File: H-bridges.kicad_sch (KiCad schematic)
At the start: 34 parts, among them J2 Conn_Coaxial, J3 Conn_Coaxial, Q10 NMOS, Q11 NMOS, Q12 NMOS, Q13 NMOS, Q14 NMOS, Q7 NMOS, Q8 NMOS, Q9 NMOS, U10 MIC4604YM, U11 MIC4604YM, U8 MIC4604YM, U9 MIC4604YM

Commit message: schematics done
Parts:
- removed D7, D8, D9: D, symbol Device:D
- added D1, D2, D5: 1N4148W, Diode_SMD:D_SOD-123, symbol Device:D
- added R1, R2: 0, Resistor_SMD:R_1206_3216Metric_Pad1.30x1.75mm_HandSolder, symbol Device:R
- D6: value D -> 1N4148W; footprint (none) -> Diode_SMD:D_SOD-123
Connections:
- net GND: now also D1.2 (A), D2.2 (A), D5.2 (A)
- net at C15.2, R35.1, U9.4 (HS): now also D1.1 (K)
- net at C14.2, R32.1, U8.4 (HS): now also D2.1 (K); no longer D6.1 (K)
- net at C16.2, R40.1, U10.4 (HS): now also D5.1 (K)
- net at C17.2, R41.1, U11.4 (HS): now also D6.1 (K)
- net P24V: no longer names the net of Q7.1 (D), Q9.1 (D)
- net P24V: now also R2.2; no longer Q11.1 (D), Q13.1 (D)
- new net: Q11.1 (D), Q13.1 (D), R1.2
- new net PHV: R1.1, R2.1

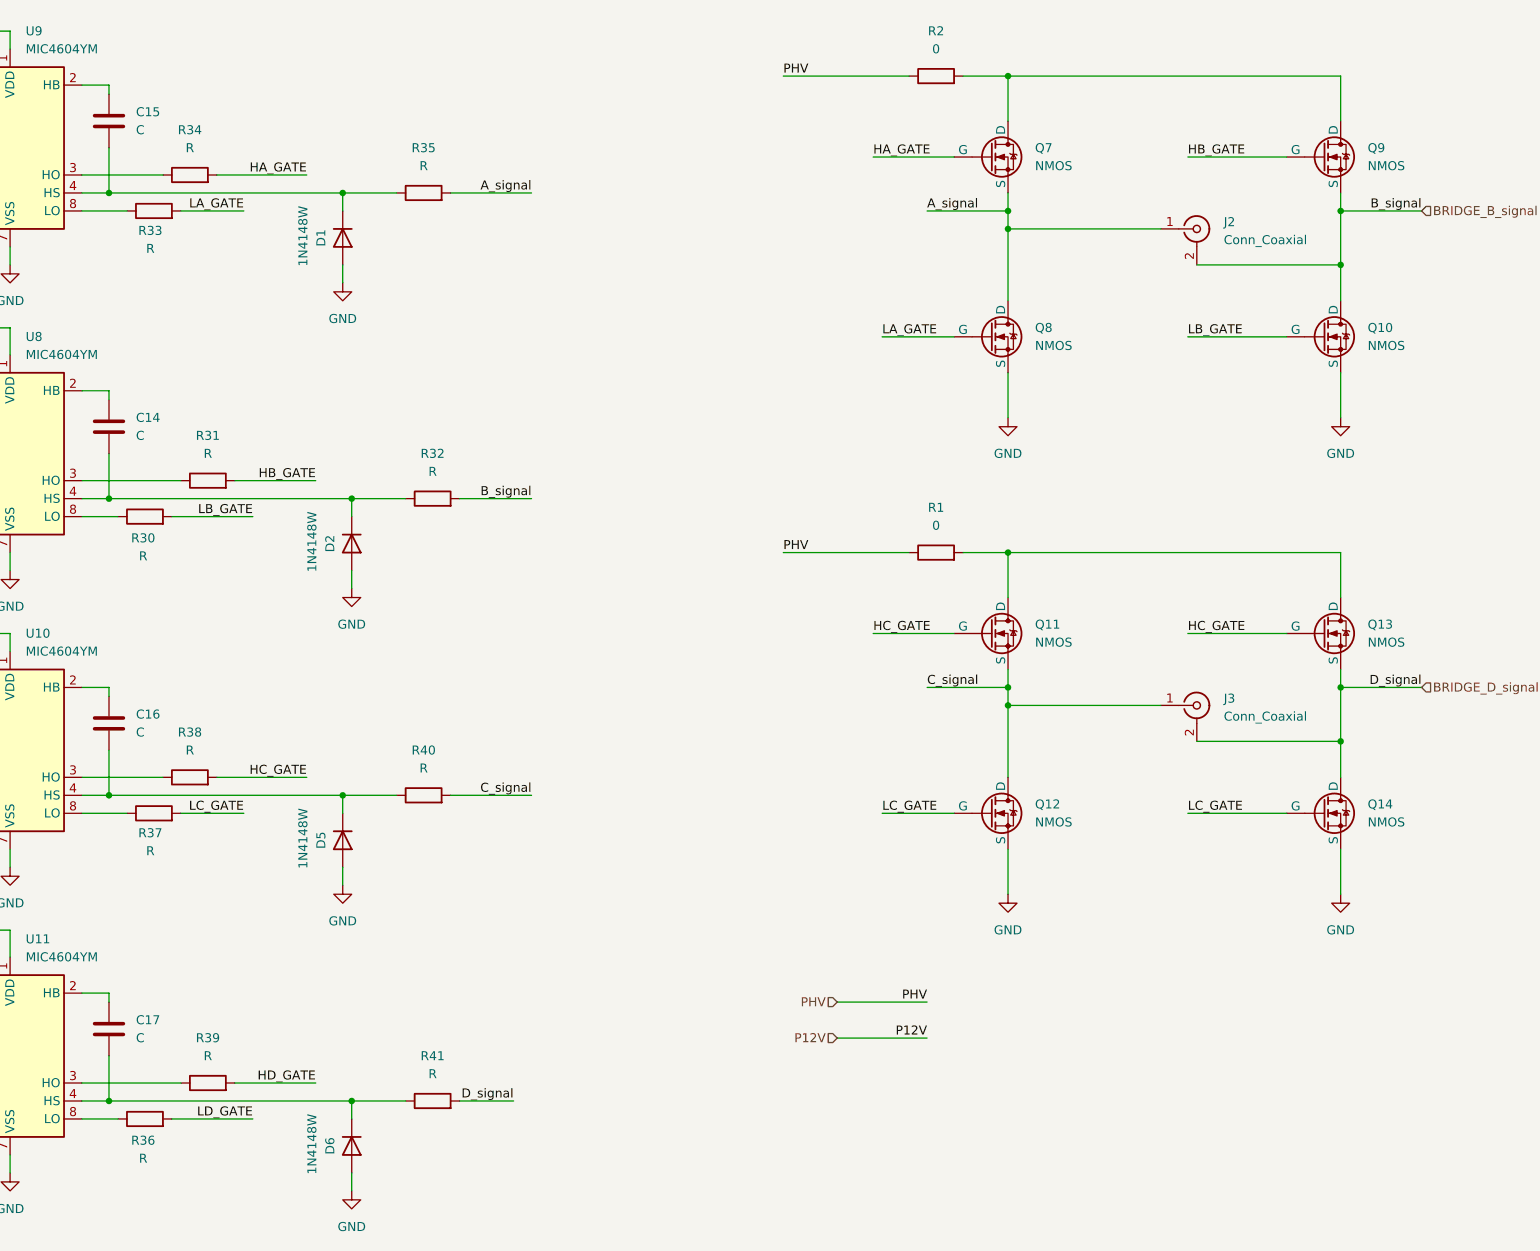
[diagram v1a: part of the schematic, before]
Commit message: ready schematic for layout
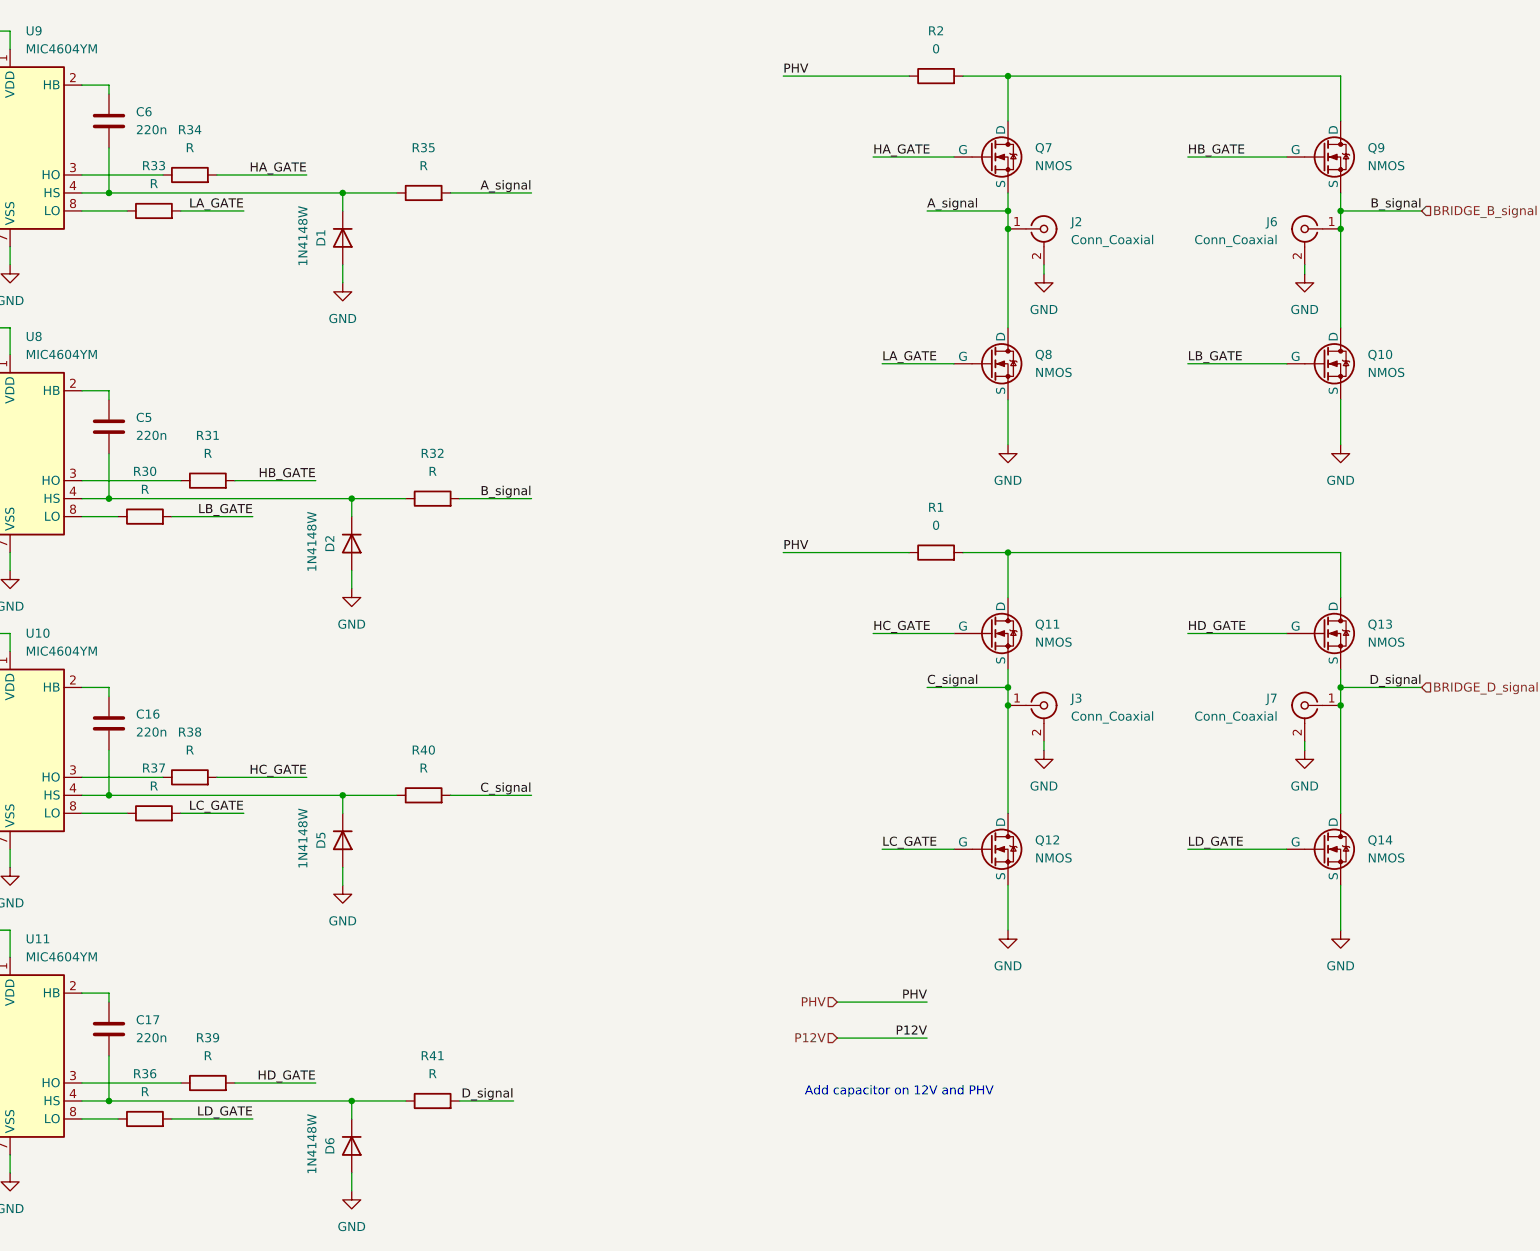
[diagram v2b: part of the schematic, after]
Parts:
- removed C14, C15: C, symbol Device:C
- added C5, C6: 220n, Capacitor_SMD:C_0603_1608Metric_Pad1.08x0.95mm_HandSolder, symbol Device:C
- added J6, J7: Conn_Coaxial, Connector_Coaxial:SMA_Amphenol_901-144_Vertical, symbol Connector:Conn_Coaxial
- C16, C17: value C -> 220n; footprint (none) -> Capacitor_SMD:C_0603_1608Metric_Pad1.08x0.95mm_HandSolder
- J2, J3: footprint (none) -> Connector_Coaxial:SMA_Amphenol_901-144_Vertical
- R30, R31, R32, R33, R34, R35, R36, R37, R38, R39, R40, R41: footprint (none) -> Resistor_SMD:R_0603_1608Metric_Pad0.98x0.95mm_HandSolder
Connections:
- net BRIDGE_B_signal: now also J6.1 (In); no longer J2.2 (Ext)
- net BRIDGE_D_signal: now also J7.1 (In); no longer J3.2 (Ext)
- net GND: now also J2.2 (Ext), J3.2 (Ext), J6.2 (Ext), J7.2 (Ext)
- net HC_GATE: no longer Q13.2 (G)
- net HD_GATE: now also Q13.2 (G)
- net LC_GATE: no longer Q14.2 (G)
- net LD_GATE: now also Q14.2 (G)
- net at D2.1 (K), R32.1, U8.4 (HS): now also C5.2
- net at U9.2 (HB): now also C6.1
- net at D1.1 (K), R35.1, U9.4 (HS): now also C6.2
- net at U8.2 (HB): now also C5.1
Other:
- note added: "Add capacitor on 12V and PHV"
- moved on the sheet: J2, Q10, Q12, Q14, Q8

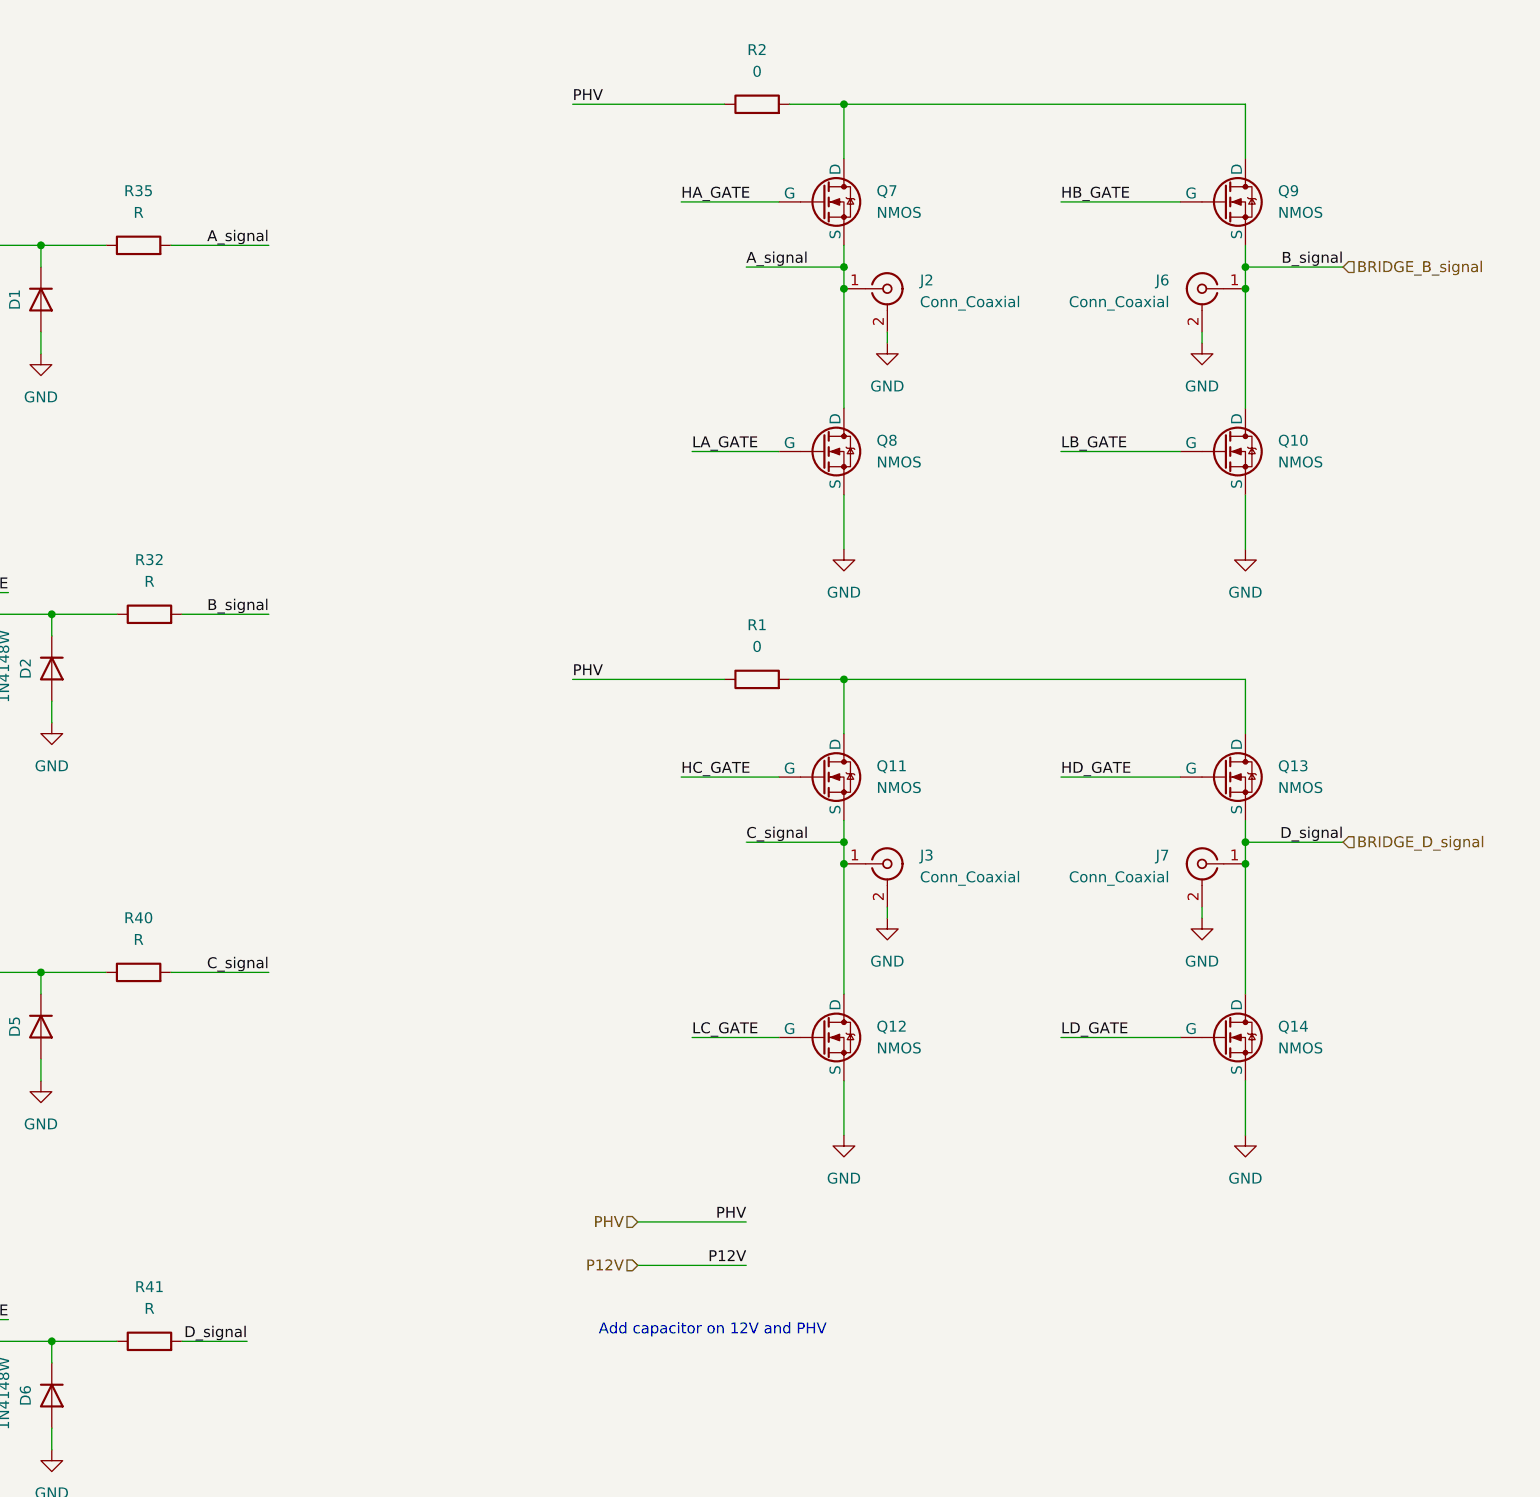
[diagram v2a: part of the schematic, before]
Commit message: new analog front end
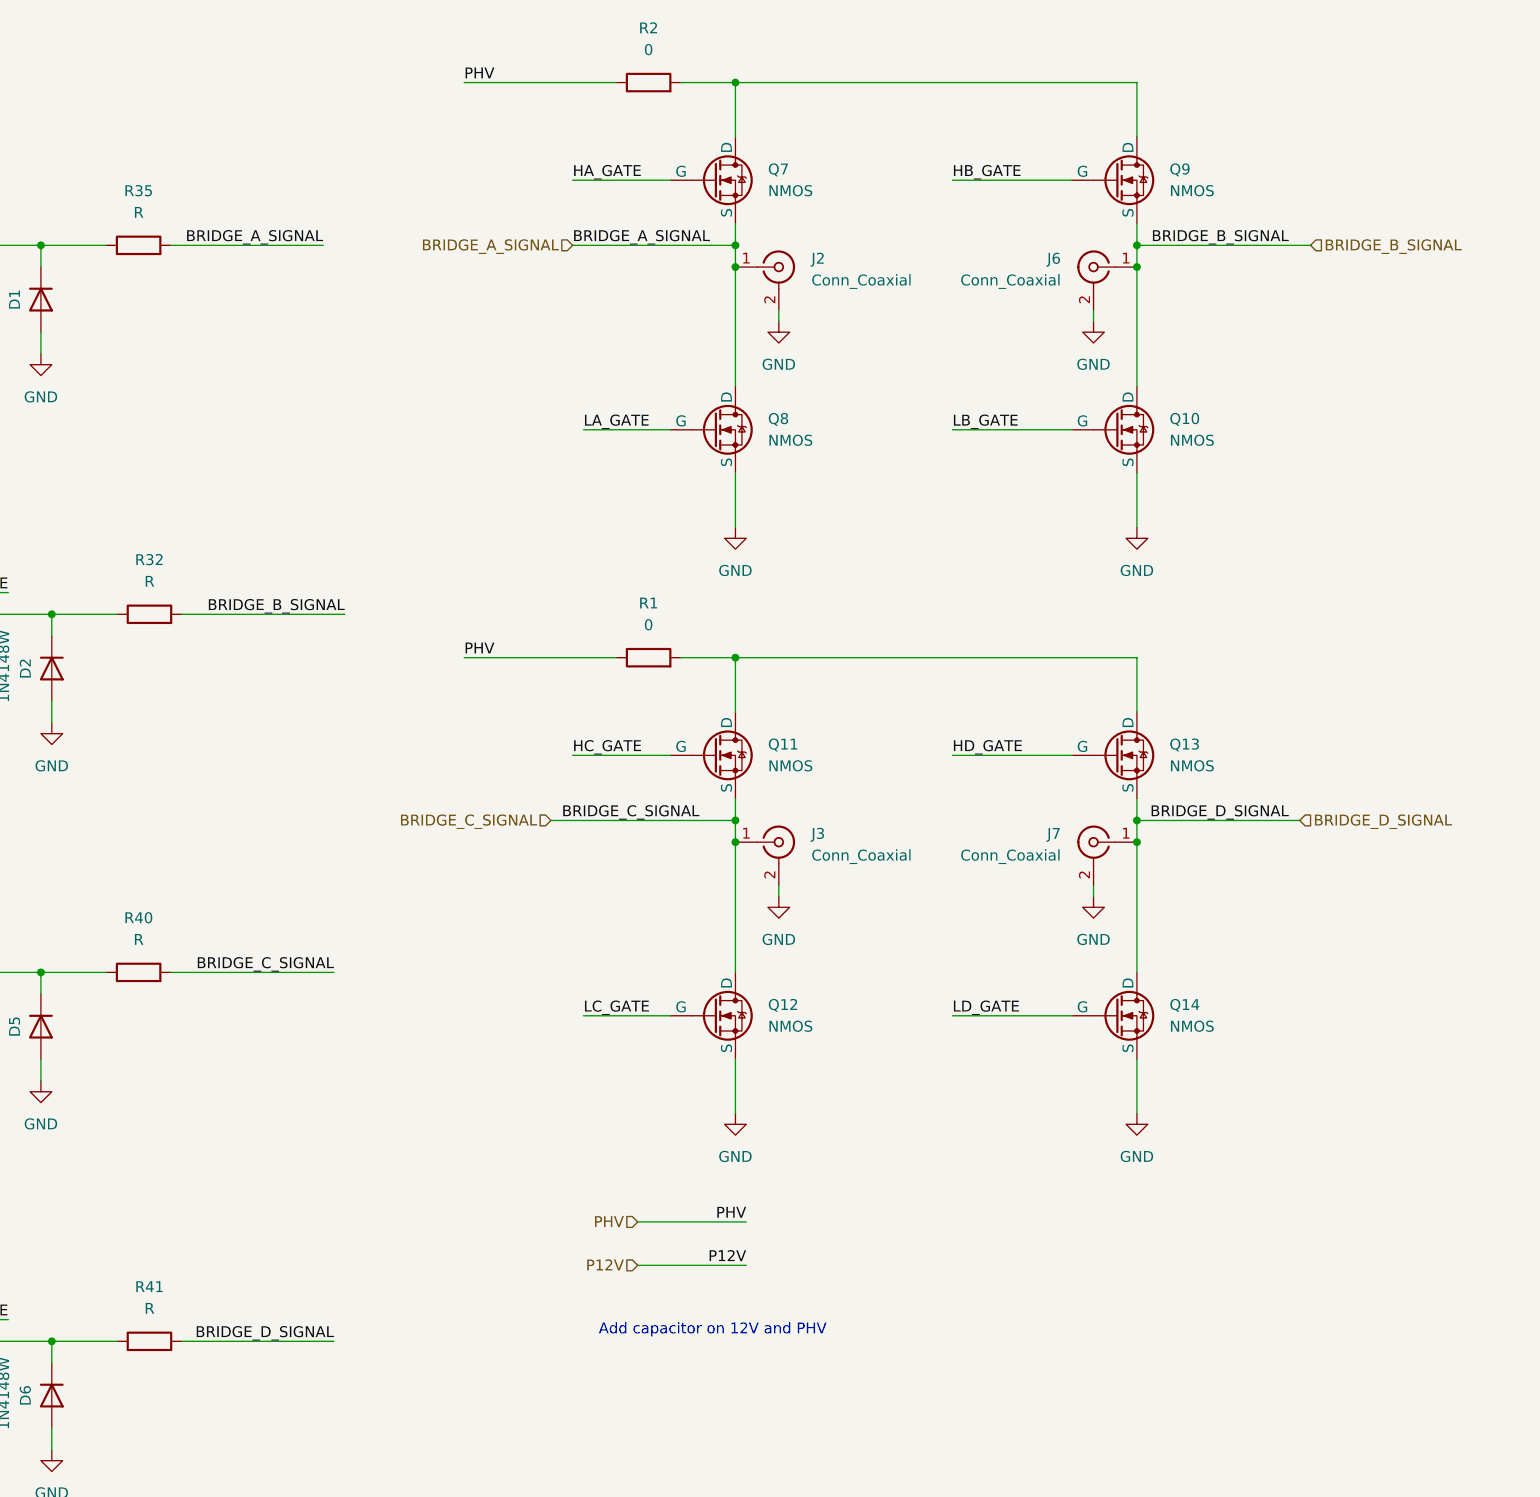
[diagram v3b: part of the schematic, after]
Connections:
- net A_signal renamed BRIDGE_A_SIGNAL
- net BRIDGE_B_signal renamed BRIDGE_B_SIGNAL
- net BRIDGE_D_signal renamed BRIDGE_D_SIGNAL
- net C_signal renamed BRIDGE_C_SIGNAL
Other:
- moved on the sheet: J2, J3, J6, J7, Q10, Q11, Q12, Q13, Q14, Q7, Q8, Q9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
